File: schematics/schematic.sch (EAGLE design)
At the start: 8 parts, among them IC1 4021N, IC2 4021N

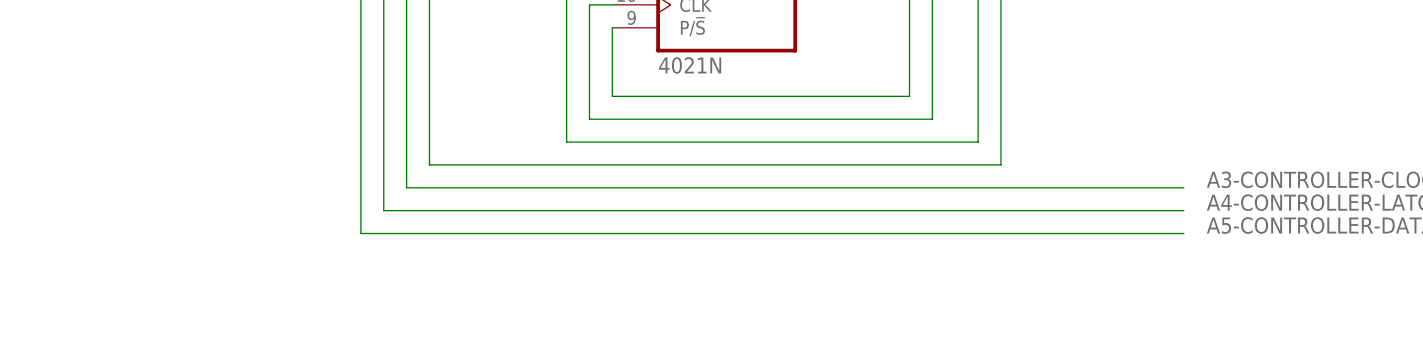
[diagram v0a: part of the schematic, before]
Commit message: Added info that +5V and GND of controller are connected to the Arduino
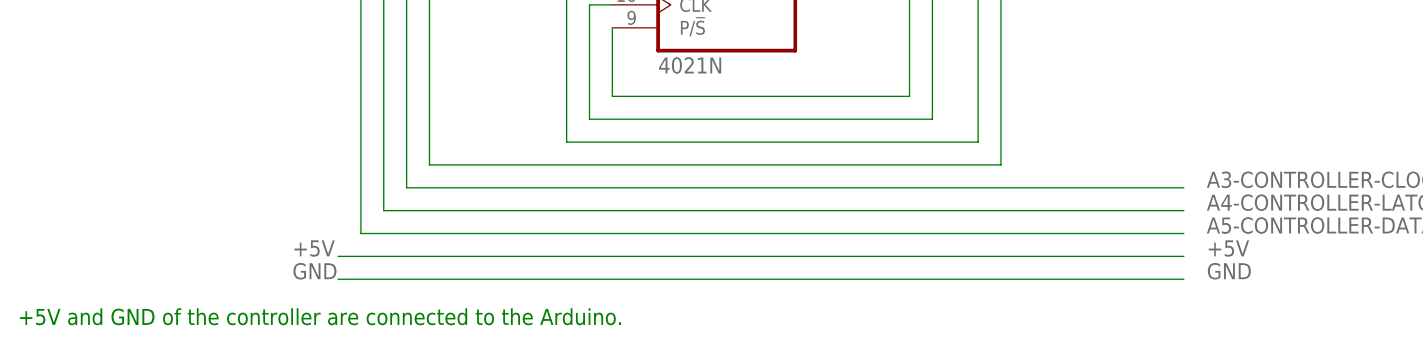
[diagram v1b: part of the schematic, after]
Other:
- note added: "+5V and GND of the controller are connected to the Arduino."
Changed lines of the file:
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@@
 2,2 kOhm for SNES-LATCH (R5)
 1 kOhm for SNES-CLOCK (R6)</text>
+<text x="-17.78" y="-27.94" size="1.778" layer="91">+5V and GND of the controller are connected to the Arduino.</text>
 </plain>
 <instances>
@@
 </segment>
 </net>
+<net name="+5V" class="0">
+<segment>
+<wire x1="111.76" y1="-20.32" x2="17.78" y2="-20.32" width="0.1524" layer="91"/>
+<label x="12.7" y="-20.32" size="1.778" layer="95"/>
+<label x="114.3" y="-20.32" size="1.778" layer="95"/>
+</segment>
+</net>
+<net name="GND" class="0">
+<segment>
+<wire x1="111.76" y1="-22.86" x2="17.78" y2="-22.86" width="0.1524" layer="91"/>
+<label x="12.7" y="-22.86" size="1.778" layer="95"/>
+<label x="114.3" y="-22.86" size="1.778" layer="95"/>
+</segment>
+</net>

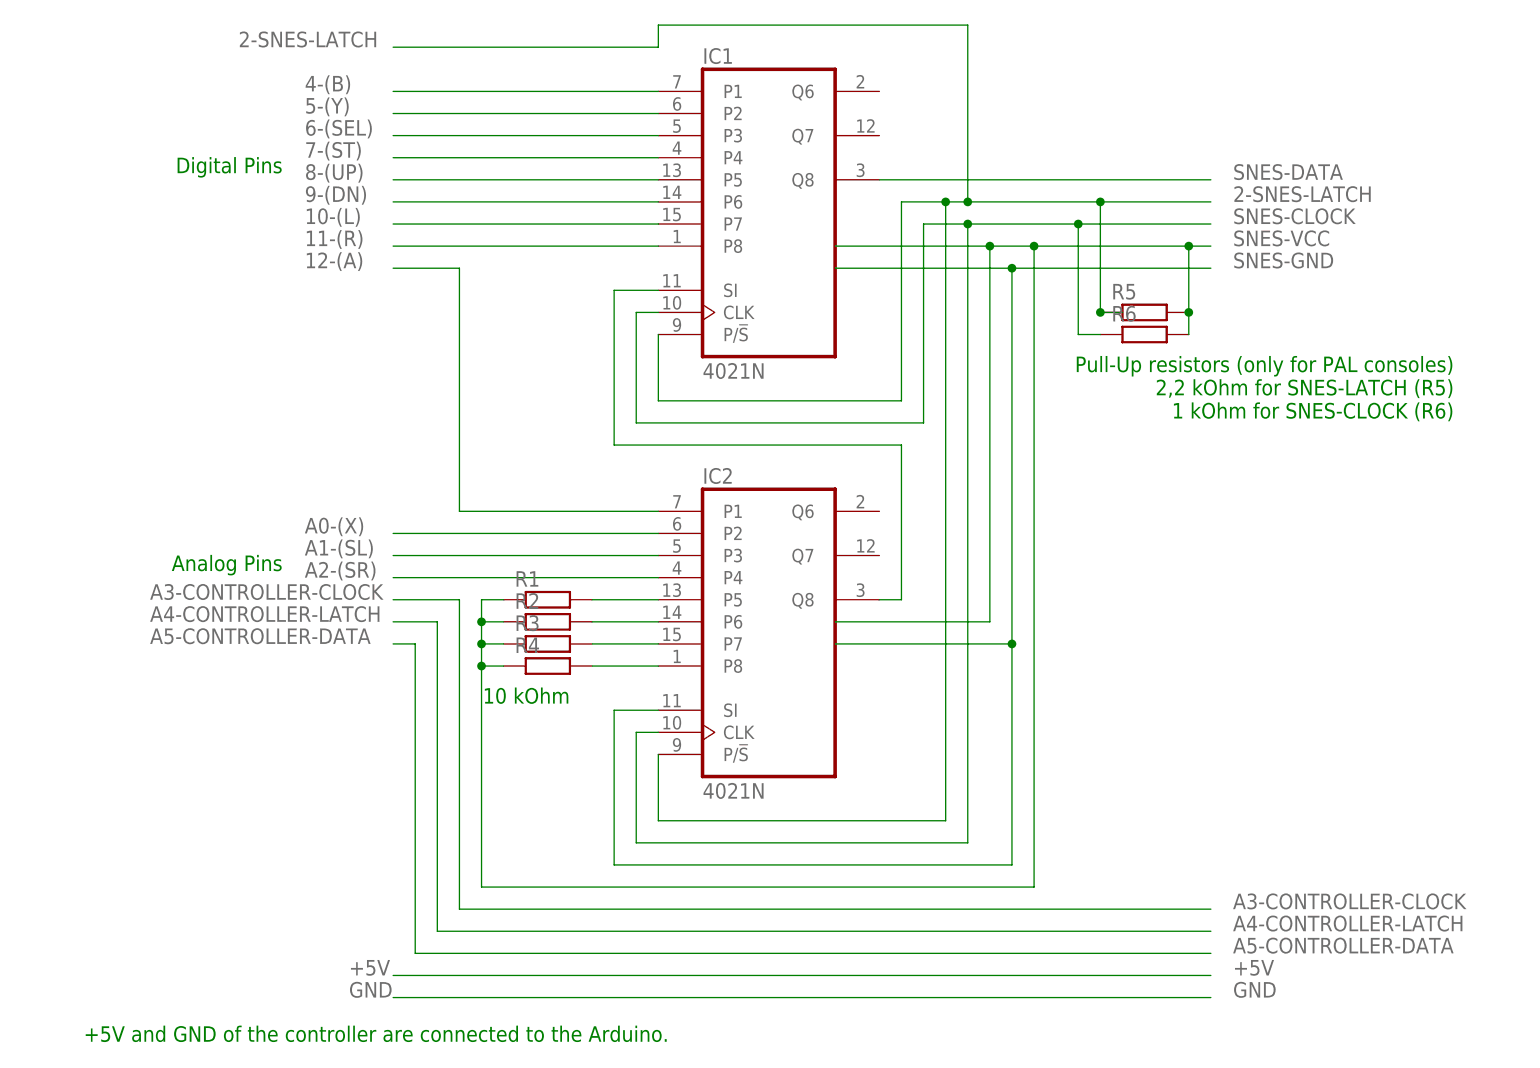
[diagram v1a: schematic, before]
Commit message: Updated schematic with common ground
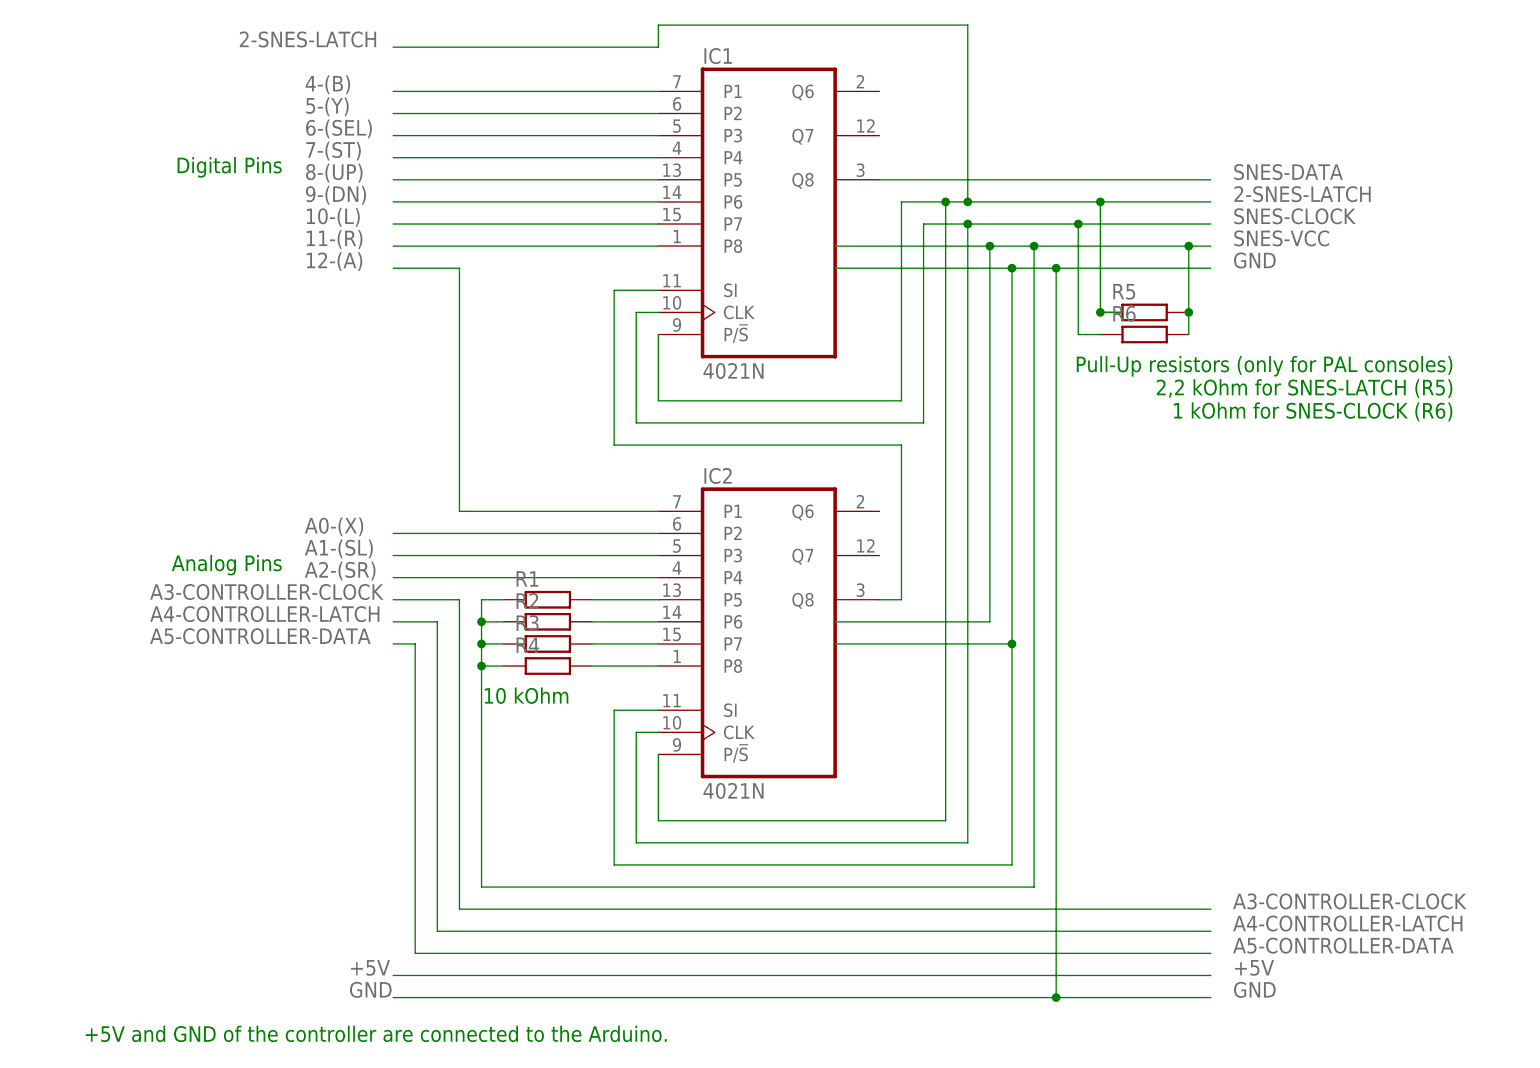
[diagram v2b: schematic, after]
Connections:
- net SNES-GND renamed GND
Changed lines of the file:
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@@
-</segment>
-</net>
-<net name="SNES-GND" class="0">
-<segment>
-<wire x1="88.9" y1="17.78" x2="88.9" y2="60.96" width="0.1524" layer="91"/>
-<wire x1="111.76" y1="60.96" x2="88.9" y2="60.96" width="0.1524" layer="91"/>
-<wire x1="68.58" y1="60.96" x2="88.9" y2="60.96" width="0.1524" layer="91"/>
-<junction x="88.9" y="60.96"/>
-<wire x1="68.58" y1="17.78" x2="88.9" y2="17.78" width="0.1524" layer="91"/>
-<label x="114.3" y="60.96" size="1.778" layer="95"/>
-<pinref part="IC2" gate="A" pin="SI"/>
-<wire x1="48.26" y1="10.16" x2="43.18" y2="10.16" width="0.1524" layer="91"/>
-<wire x1="43.18" y1="10.16" x2="43.18" y2="-7.62" width="0.1524" layer="91"/>
-<wire x1="43.18" y1="-7.62" x2="88.9" y2="-7.62" width="0.1524" layer="91"/>
-<wire x1="88.9" y1="-7.62" x2="88.9" y2="17.78" width="0.1524" layer="91"/>
-<junction x="88.9" y="17.78"/>
 </segment>
 </net>
@@
 <net name="GND" class="0">
 <segment>
-<wire x1="111.76" y1="-22.86" x2="17.78" y2="-22.86" width="0.1524" layer="91"/>
+<wire x1="88.9" y1="17.78" x2="88.9" y2="60.96" width="0.1524" layer="91"/>
+<wire x1="111.76" y1="60.96" x2="93.98" y2="60.96" width="0.1524" layer="91"/>
+<wire x1="93.98" y1="60.96" x2="88.9" y2="60.96" width="0.1524" layer="91"/>
+<wire x1="68.58" y1="60.96" x2="88.9" y2="60.96" width="0.1524" layer="91"/>
+<junction x="88.9" y="60.96"/>
+<wire x1="68.58" y1="17.78" x2="88.9" y2="17.78" width="0.1524" layer="91"/>
+<label x="114.3" y="60.96" size="1.778" layer="95"/>
+<pinref part="IC2" gate="A" pin="SI"/>
+<wire x1="48.26" y1="10.16" x2="43.18" y2="10.16" width="0.1524" layer="91"/>
+<wire x1="43.18" y1="10.16" x2="43.18" y2="-7.62" width="0.1524" layer="91"/>
+<wire x1="43.18" y1="-7.62" x2="88.9" y2="-7.62" width="0.1524" layer="91"/>
+<wire x1="88.9" y1="-7.62" x2="88.9" y2="17.78" width="0.1524" layer="91"/>
+<junction x="88.9" y="17.78"/>
+<wire x1="111.76" y1="-22.86" x2="93.98" y2="-22.86" width="0.1524" layer="91"/>
 <label x="12.7" y="-22.86" size="1.778" layer="95"/>
 <label x="114.3" y="-22.86" size="1.778" layer="95"/>
+<wire x1="93.98" y1="-22.86" x2="17.78" y2="-22.86" width="0.1524" layer="91"/>
+<wire x1="93.98" y1="60.96" x2="93.98" y2="-22.86" width="0.1524" layer="91"/>
+<junction x="93.98" y="60.96"/>
+<junction x="93.98" y="-22.86"/>
 </segment>
 </net>

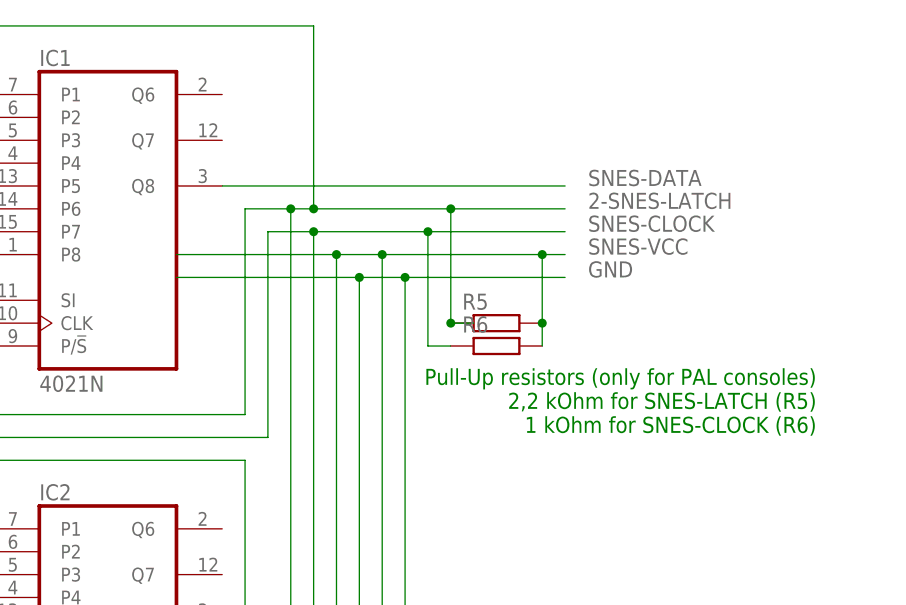
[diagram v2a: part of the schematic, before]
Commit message: Added diode to prevent current from running back into the console
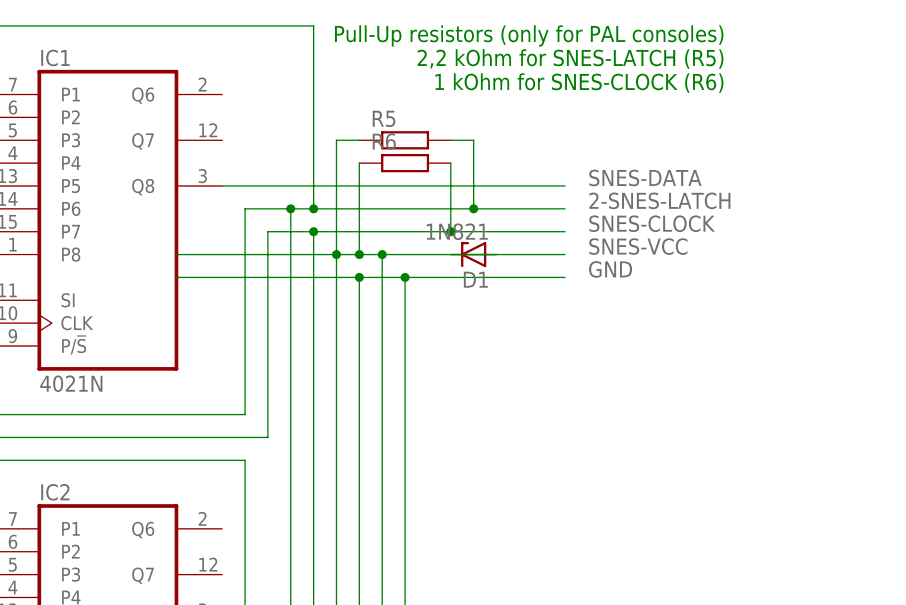
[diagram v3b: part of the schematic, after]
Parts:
- added D1: 1N821, diode:1N821
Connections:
- new net N$5: D1.C
- net 2-SNES-LATCH: now also R5.2; no longer R5.1
- net SNES-CLOCK: now also R6.2; no longer R6.1
- net SNES-VCC: now also D1.A, R5.1, R6.1; no longer R5.2, R6.2
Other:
- moved on the sheet: R5, R6
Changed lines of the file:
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@@
 <part name="R5" library="rcl" library_urn="urn:adsk.eagle:library:334" deviceset="R-EU_" device="0204/2V" package3d_urn="urn:adsk.eagle:package:23495/1"/>
 <part name="R6" library="rcl" library_urn="urn:adsk.eagle:library:334" deviceset="R-EU_" device="0204/2V" package3d_urn="urn:adsk.eagle:package:23495/1"/>
+<part name="D1" library="diode" library_urn="urn:adsk.eagle:library:210" deviceset="1N821" device="" package3d_urn="urn:adsk.eagle:package:43342/1"/>
 </parts>
 <sheets>
@@
 <text x="5.08" y="27.94" size="1.778" layer="91" rot="R180">Analog Pins</text>
 <text x="38.1" y="12.7" size="1.778" layer="91" rot="R180">10 kOhm</text>
-<text x="139.7" y="50.8" size="1.778" layer="91" rot="R180">Pull-Up resistors (only for PAL consoles)
+<text x="129.54" y="88.9" size="1.778" layer="91" rot="R180">Pull-Up resistors (only for PAL consoles)
 2,2 kOhm for SNES-LATCH (R5)
 1 kOhm for SNES-CLOCK (R6)</text>
@@
 <instance part="R3" gate="G$1" x="35.56" y="17.78"/>
 <instance part="R4" gate="G$1" x="35.56" y="15.24"/>
-<instance part="R5" gate="G$1" x="104.14" y="55.88">
-<attribute name="SPICEPREFIX" x="104.14" y="55.88" size="1.778" layer="96" display="off"/>
+<instance part="R5" gate="G$1" x="93.98" y="76.2">
+<attribute name="SPICEPREFIX" x="93.98" y="76.2" size="1.778" layer="96" display="off"/>
 </instance>
-<instance part="R6" gate="G$1" x="104.14" y="53.34">
-<attribute name="SPICEPREFIX" x="104.14" y="53.34" size="1.778" layer="96" display="off"/>
+<instance part="R6" gate="G$1" x="93.98" y="73.66">
+<attribute name="SPICEPREFIX" x="93.98" y="73.66" size="1.778" layer="96" display="off"/>
 </instance>
+<instance part="D1" gate="1" x="101.6" y="63.5" rot="R180"/>
 </instances>
 <busses>
@@
 <pinref part="IC2" gate="A" pin="P/!S"/>
 <wire x1="81.28" y1="68.58" x2="83.82" y2="68.58" width="0.1524" layer="91"/>
-<wire x1="83.82" y1="68.58" x2="99.06" y2="68.58" width="0.1524" layer="91"/>
-<wire x1="99.06" y1="68.58" x2="111.76" y2="68.58" width="0.1524" layer="91"/>
+<wire x1="83.82" y1="68.58" x2="101.6" y2="68.58" width="0.1524" layer="91"/>
+<wire x1="101.6" y1="68.58" x2="111.76" y2="68.58" width="0.1524" layer="91"/>
 <wire x1="48.26" y1="5.08" x2="48.26" y2="-2.54" width="0.1524" layer="91"/>
 <wire x1="48.26" y1="-2.54" x2="81.28" y2="-2.54" width="0.1524" layer="91"/>
 <wire x1="81.28" y1="-2.54" x2="81.28" y2="68.58" width="0.1524" layer="91"/>
 <junction x="81.28" y="68.58"/>
-<pinref part="R5" gate="G$1" pin="1"/>
-<wire x1="99.06" y1="55.88" x2="101.6" y2="55.88" width="0.1524" layer="91"/>
-<wire x1="99.06" y1="55.88" x2="99.06" y2="68.58" width="0.1524" layer="91"/>
-<junction x="99.06" y="55.88"/>
-<junction x="99.06" y="68.58"/>
 <label x="0" y="86.36" size="1.778" layer="95"/>
 <wire x1="83.82" y1="88.9" x2="83.82" y2="68.58" width="0.1524" layer="91"/>
@@
 <wire x1="48.26" y1="88.9" x2="48.26" y2="86.36" width="0.1524" layer="91"/>
 <wire x1="48.26" y1="86.36" x2="17.78" y2="86.36" width="0.1524" layer="91"/>
+<pinref part="R5" gate="G$1" pin="2"/>
+<wire x1="99.06" y1="76.2" x2="101.6" y2="76.2" width="0.1524" layer="91"/>
+<wire x1="101.6" y1="68.58" x2="101.6" y2="76.2" width="0.1524" layer="91"/>
+<junction x="101.6" y="68.58"/>
 </segment>
 </net>
@@
 <label x="114.3" y="66.04" size="1.778" layer="95"/>
 <pinref part="IC2" gate="A" pin="CLK"/>
-<wire x1="83.82" y1="66.04" x2="96.52" y2="66.04" width="0.1524" layer="91"/>
-<wire x1="96.52" y1="66.04" x2="111.76" y2="66.04" width="0.1524" layer="91"/>
+<wire x1="83.82" y1="66.04" x2="99.06" y2="66.04" width="0.1524" layer="91"/>
+<wire x1="99.06" y1="66.04" x2="111.76" y2="66.04" width="0.1524" layer="91"/>
 <wire x1="48.26" y1="7.62" x2="45.72" y2="7.62" width="0.1524" layer="91"/>
 <wire x1="45.72" y1="7.62" x2="45.72" y2="-5.08" width="0.1524" layer="91"/>
@@
 <wire x1="83.82" y1="-5.08" x2="83.82" y2="66.04" width="0.1524" layer="91"/>
 <junction x="83.82" y="66.04"/>
-<pinref part="R6" gate="G$1" pin="1"/>
-<wire x1="99.06" y1="53.34" x2="96.52" y2="53.34" width="0.1524" layer="91"/>
-<wire x1="96.52" y1="53.34" x2="96.52" y2="66.04" width="0.1524" layer="91"/>
-<junction x="96.52" y="66.04"/>
+<pinref part="R6" gate="G$1" pin="2"/>
+<wire x1="99.06" y1="73.66" x2="99.06" y2="66.04" width="0.1524" layer="91"/>
+<junction x="99.06" y="66.04"/>
 </segment>
 </net>
@@
 <net name="SNES-VCC" class="0">
 <segment>
-<wire x1="111.76" y1="63.5" x2="109.22" y2="63.5" width="0.1524" layer="91"/>
-<wire x1="109.22" y1="63.5" x2="91.44" y2="63.5" width="0.1524" layer="91"/>
-<wire x1="91.44" y1="63.5" x2="86.36" y2="63.5" width="0.1524" layer="91"/>
+<wire x1="91.44" y1="63.5" x2="88.9" y2="63.5" width="0.1524" layer="91"/>
+<wire x1="88.9" y1="63.5" x2="86.36" y2="63.5" width="0.1524" layer="91"/>
 <wire x1="86.36" y1="63.5" x2="68.58" y2="63.5" width="0.1524" layer="91"/>
 <wire x1="68.58" y1="20.32" x2="86.36" y2="20.32" width="0.1524" layer="91"/>
@@
 <wire x1="27.94" y1="-10.16" x2="91.44" y2="-10.16" width="0.1524" layer="91"/>
 <wire x1="91.44" y1="-10.16" x2="91.44" y2="63.5" width="0.1524" layer="91"/>
+<pinref part="R6" gate="G$1" pin="1"/>
+<wire x1="88.9" y1="73.66" x2="88.9" y2="63.5" width="0.1524" layer="91"/>
+<junction x="88.9" y="63.5"/>
+<pinref part="R5" gate="G$1" pin="1"/>
+<wire x1="88.9" y1="76.2" x2="86.36" y2="76.2" width="0.1524" layer="91"/>
+<wire x1="86.36" y1="76.2" x2="86.36" y2="63.5" width="0.1524" layer="91"/>
+<wire x1="91.44" y1="63.5" x2="104.14" y2="63.5" width="0.1524" layer="91"/>
 <junction x="91.44" y="63.5"/>
-<pinref part="R5" gate="G$1" pin="2"/>
-<wire x1="109.22" y1="55.88" x2="109.22" y2="63.5" width="0.1524" layer="91"/>
-<junction x="109.22" y="63.5"/>
-<pinref part="R6" gate="G$1" pin="2"/>
-<wire x1="109.22" y1="53.34" x2="109.22" y2="55.88" width="0.1524" layer="91"/>
-<junction x="109.22" y="55.88"/>
+<pinref part="D1" gate="1" pin="A"/>
 </segment>
 </net>
@@
 </segment>
 </net>
+<net name="N$5" class="0">
+<segment>
+<pinref part="D1" gate="1" pin="C"/>
+<wire x1="99.06" y1="63.5" x2="111.76" y2="63.5" width="0.1524" layer="91"/>
+</segment>
+</net>

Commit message: Added note about incorrect pinout
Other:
- note added: "Note: P1-P8 are incorrectly based on the chips pinout (so P1 = 1, P2 = 2, etc...)"
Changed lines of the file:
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@@
 1 kOhm for SNES-CLOCK (R6)</text>
 <text x="-17.78" y="-27.94" size="1.778" layer="91">+5V and GND of the controller are connected to the Arduino.</text>
+<text x="-25.4" y="43.18" size="1.778" layer="91">Note: P1-P8 are incorrectly based on
+the chips pinout (so P1 = 1, P2 = 2, etc...)</text>
 </plain>
 <instances>
